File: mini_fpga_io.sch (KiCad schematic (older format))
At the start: 1 part

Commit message: First checkover of schematic complete, should be working.
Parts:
- added D? (x3): LED, ~, symbol LED
- added J? (x2): 1X6_HEADER, symbol 1X6_HEADER
- added R? (x3): 330, ~, symbol R
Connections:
- net at U?.F11 (IO_L31P_A19_M1CKE_1): now also D?.1 (A)
- net at U?.F12 (IO_L31N_A18_M1A12_1): now also D?.1 (A)
- net at U?.F13 (IO_L39P_M1A3_1): now also J?.1 (D1)
- net at U?.F15 (IO_L39N_M1ODT_1): now also J?.2 (D2)
- net at U?.H10 (IO_L32P_A17_M1A8_1): now also D?.1 (A)
- net at U?.K12 (IO_L40P_GCLK11_M1A5_1): now also J?.3 (D3)
- net at U?.L12 (IO_L40N_GCLK10_M1A6_1): now also J?.4 (D4)
- net at U?.L14 (IO_L45P_A1_M1LDQS_1): now also J?.1 (D1)
- net at U?.L15 (IO_L45N_A0_M1LDQSN_1): now also J?.2 (D2)
- net at U?.M13 (IO_L46P_FCS_B_M1DQ2_1): now also J?.3 (D3)
- net at U?.M15 (IO_L46N_FOE_B_M1DQ3_1): now also J?.4 (D4)
- new net: D?.2 (K), R?.2 (x3)
- new net +3.3V: J?.6 (VCC), J?.6 (VCC)
- new net GND: J?.5 (GND), J?.5 (GND), R?.1, R?.1, R?.1
- no-connect marks 1 -> 29
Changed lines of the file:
@@
 Sheet 4 6
 Title ""
-Date "26 jul 2014"
+Date "28 jul 2014"
 Rev ""
 Comp ""
@@
 $EndComp
 NoConn ~ 8700 4800
+$Comp
+L 1X6_HEADER J?
+U 1 1 53D596A7
+P 10200 2250
+F 0 "J?" H 10250 2650 60  0000 C CNN
+F 1 "1X6_HEADER" H 10350 1850 60  0000 C CNN
+F 2 "" H 10300 2000 60  0000 C CNN
+F 3 "" H 10300 2000 60  0000 C CNN
+	1    10200 2250
+	1    0    0    -1
+$EndComp
+$Comp
+L 1X6_HEADER J?
+U 1 1 53D596B4
+P 10200 4050
+F 0 "J?" H 10250 4450 60  0000 C CNN
+F 1 "1X6_HEADER" H 10350 3650 60  0000 C CNN
+F 2 "" H 10300 3800 60  0000 C CNN
+F 3 "" H 10300 3800 60  0000 C CNN
+	1    10200 4050
+	1    0    0    -1
+$EndComp
+Wire Wire Line
+	9900 3800 8700 3800
+Wire Wire Line
+	9900 3900 8700 3900
+Wire Wire Line
+	9900 4000 8850 4000
+Wire Wire Line
+	8850 4000 8850 4100
+Wire Wire Line
+	8850 4100 8700 4100
+Wire Wire Line
+	9900 4100 8950 4100
+Wire Wire Line
+	8950 4100 8950 4200
+Wire Wire Line
+	8950 4200 8700 4200
+Wire Wire Line
+	9900 4200 9050 4200
+Wire Wire Line
+	9050 2400 9050 4350
+Wire Wire Line
+	9800 4300 9900 4300
+Wire Wire Line
+	9800 2500 9800 4300
+Wire Wire Line
+	9900 2000 8700 2000
+Wire Wire Line
+	9900 2100 8700 2100
+Wire Wire Line
+	9900 2200 8850 2200
+Wire Wire Line
+	8850 2200 8850 2300
+Wire Wire Line
+	8850 2300 8700 2300
+Wire Wire Line
+	9900 2300 8950 2300
+Wire Wire Line
+	8950 2300 8950 2400
+Wire Wire Line
+	8950 2400 8700 2400
+Wire Wire Line
+	9900 2500 9800 2500
+$Comp
+L +3.3V #PWR?
+U 1 1 53D59B4F
+P 10250 3100
+F 0 "#PWR?" H 10250 3060 30  0001 C CNN
+F 1 "+3.3V" H 10250 3210 30  0000 C CNN
+F 2 "" H 10250 3100 60  0000 C CNN
+F 3 "" H 10250 3100 60  0000 C CNN
+	1    10250 3100
+	1    0    0    -1
+$EndComp
+Wire Wire Line
+	10250 3100 10250 3200
+Wire Wire Line
+	10250 3200 9800 3200
+Connection ~ 9800 3200
+Wire Wire Line
+	9900 2400 9050 2400
+Connection ~ 9050 4200
+$Comp
+L GND #PWR?
+U 1 1 53D59B8D
+P 9050 4350
+F 0 "#PWR?" H 9050 4350 30  0001 C CNN
+F 1 "GND" H 9050 4280 30  0001 C CNN
+F 2 "" H 9050 4350 60  0000 C CNN
+F 3 "" H 9050 4350 60  0000 C CNN
+	1    9050 4350
+	1    0    0    -1
+$EndComp
+NoConn ~ 8700 2600
+NoConn ~ 8700 2700
+NoConn ~ 8700 2900
+NoConn ~ 8700 3000
+NoConn ~ 8700 3200
+NoConn ~ 8700 3300
+NoConn ~ 8700 3500
+NoConn ~ 8700 3600
+NoConn ~ 8700 4400
+NoConn ~ 8700 4500
+NoConn ~ 8700 4700
+NoConn ~ 5700 4800
+NoConn ~ 5700 4700
+NoConn ~ 5700 4500
+NoConn ~ 5700 4400
+NoConn ~ 5700 4200
+NoConn ~ 5700 4100
+NoConn ~ 5700 3900
+NoConn ~ 5700 3800
+NoConn ~ 5700 3600
+NoConn ~ 5700 3500
+NoConn ~ 5700 3300
+NoConn ~ 5700 3200
+NoConn ~ 5700 3000
+NoConn ~ 5700 2400
+NoConn ~ 5700 2300
+NoConn ~ 5700 2100
+NoConn ~ 5700 2000
+$Comp
+L LED D?
+U 1 1 53D5A712
+P 4900 2600
+F 0 "D?" H 4900 2700 50  0000 C CNN
+F 1 "LED" H 4900 2500 50  0000 C CNN
+F 2 "~" H 4900 2600 60  0000 C CNN
+F 3 "~" H 4900 2600 60  0000 C CNN
+	1    4900 2600
+	-1   0    0    1
+$EndComp
+$Comp
+L LED D?
+U 1 1 53D5A71F
+P 4900 2900
+F 0 "D?" H 4900 3000 50  0000 C CNN
+F 1 "LED" H 4900 2800 50  0000 C CNN
+F 2 "~" H 4900 2900 60  0000 C CNN
+F 3 "~" H 4900 2900 60  0000 C CNN
+	1    4900 2900
+	-1   0    0    1
+$EndComp
+$Comp
+L LED D?
+U 1 1 53D5A725
+P 4900 3200
+F 0 "D?" H 4900 3300 50  0000 C CNN
+F 1 "LED" H 4900 3100 50  0000 C CNN
+F 2 "~" H 4900 3200 60  0000 C CNN
+F 3 "~" H 4900 3200 60  0000 C CNN
+	1    4900 3200
+	-1   0    0    1
+$EndComp
+$Comp
+L GND #PWR?
+U 1 1 53D5A72D
+P 3650 3500
+F 0 "#PWR?" H 3650 3500 30  0001 C CNN
+F 1 "GND" H 3650 3430 30  0001 C CNN
+F 2 "" H 3650 3500 60  0000 C CNN
+F 3 "" H 3650 3500 60  0000 C CNN
+	1    3650 3500
+	1    0    0    -1
+$EndComp
+$Comp
+L R R?
+U 1 1 53D5A73C
+P 4100 2600
+F 0 "R?" V 4180 2600 40  0000 C CNN
+F 1 "330" V 4107 2601 40  0000 C CNN
+F 2 "~" V 4030 2600 30  0000 C CNN
+F 3 "~" H 4100 2600 30  0000 C CNN
+	1    4100 2600
+	0    -1   -1   0
+$EndComp
+Wire Wire Line
+	3850 2600 3650 2600
+Wire Wire Line
+	3650 2600 3650 3500
+Wire Wire Line
+	3850 2900 3650 2900
+Connection ~ 3650 2900
+Wire Wire Line
+	3850 3200 3650 3200
+Connection ~ 3650 3200
+Wire Wire Line
+	4700 2600 4350 2600
+$Comp
+L R R?
+U 1 1 53D5A7E5
+P 4100 2900
+F 0 "R?" V 4180 2900 40  0000 C CNN
+F 1 "330" V 4107 2901 40  0000 C CNN
+F 2 "~" V 4030 2900 30  0000 C CNN
+F 3 "~" H 4100 2900 30  0000 C CNN
+	1    4100 2900
+	0    -1   -1   0
+$EndComp
+$Comp
+L R R?
+U 1 1 53D5A7EB
+P 4100 3200
+F 0 "R?" V 4180 3200 40  0000 C CNN
+F 1 "330" V 4107 3201 40  0000 C CNN
+F 2 "~" V 4030 3200 30  0000 C CNN
+F 3 "~" H 4100 3200 30  0000 C CNN
+	1    4100 3200
+	0    -1   -1   0
+$EndComp
+Wire Wire Line
+	4350 2900 4700 2900
+Wire Wire Line
+	4350 3200 4700 3200
+Wire Wire Line
+	5100 2600 5700 2600
+Wire Wire Line
+	5100 2900 5100 2700
+Wire Wire Line
+	5100 2700 5700 2700
+Wire Wire Line
+	5100 3200 5200 3200
+Wire Wire Line
+	5200 3200 5200 2900
+Wire Wire Line
+	5200 2900 5700 2900
 $EndSCHEMATC

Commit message: Annotated!
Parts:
- gave numbers to parts that had none: 9
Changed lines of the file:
@@
 $EndDescr
 $Comp
-L XC6SLX9 U?
+L XC6SLX9 U3
 U 4 1 53CA82DC
 P 7200 3250
-F 0 "U?" H 7200 3150 60  0000 C CNN
+F 0 "U3" H 7200 3150 60  0000 C CNN
 F 1 "XC6SLX9" H 7200 3350 60  0000 C CNN
 F 2 "~" H 7350 5250 60  0000 C CNN
@@
 NoConn ~ 8700 4800
 $Comp
-L 1X6_HEADER J?
+L 1X6_HEADER J2
 U 1 1 53D596A7
 P 10200 2250
-F 0 "J?" H 10250 2650 60  0000 C CNN
+F 0 "J2" H 10250 2650 60  0000 C CNN
 F 1 "1X6_HEADER" H 10350 1850 60  0000 C CNN
 F 2 "" H 10300 2000 60  0000 C CNN
@@
 $EndComp
 $Comp
-L 1X6_HEADER J?
+L 1X6_HEADER J3
 U 1 1 53D596B4
 P 10200 4050
-F 0 "J?" H 10250 4450 60  0000 C CNN
+F 0 "J3" H 10250 4450 60  0000 C CNN
 F 1 "1X6_HEADER" H 10350 3650 60  0000 C CNN
 F 2 "" H 10300 3800 60  0000 C CNN
@@
 	9900 2500 9800 2500
 $Comp
-L +3.3V #PWR?
+L +3.3V #PWR39
 U 1 1 53D59B4F
 P 10250 3100
-F 0 "#PWR?" H 10250 3060 30  0001 C CNN
+F 0 "#PWR39" H 10250 3060 30  0001 C CNN
 F 1 "+3.3V" H 10250 3210 30  0000 C CNN
 F 2 "" H 10250 3100 60  0000 C CNN
@@
 Connection ~ 9050 4200
 $Comp
-L GND #PWR?
+L GND #PWR38
 U 1 1 53D59B8D
 P 9050 4350
-F 0 "#PWR?" H 9050 4350 30  0001 C CNN
+F 0 "#PWR38" H 9050 4350 30  0001 C CNN
 F 1 "GND" H 9050 4280 30  0001 C CNN
 F 2 "" H 9050 4350 60  0000 C CNN
@@
 NoConn ~ 5700 2000
 $Comp
-L LED D?
+L LED D2
 U 1 1 53D5A712
 P 4900 2600
-F 0 "D?" H 4900 2700 50  0000 C CNN
+F 0 "D2" H 4900 2700 50  0000 C CNN
 F 1 "LED" H 4900 2500 50  0000 C CNN
 F 2 "~" H 4900 2600 60  0000 C CNN
@@
 $EndComp
 $Comp
-L LED D?
+L LED D3
 U 1 1 53D5A71F
 P 4900 2900
-F 0 "D?" H 4900 3000 50  0000 C CNN
+F 0 "D3" H 4900 3000 50  0000 C CNN
 F 1 "LED" H 4900 2800 50  0000 C CNN
 F 2 "~" H 4900 2900 60  0000 C CNN
@@
 $EndComp
 $Comp
-L LED D?
+L LED D4
 U 1 1 53D5A725
 P 4900 3200
-F 0 "D?" H 4900 3300 50  0000 C CNN
+F 0 "D4" H 4900 3300 50  0000 C CNN
 F 1 "LED" H 4900 3100 50  0000 C CNN
 F 2 "~" H 4900 3200 60  0000 C CNN
@@
 $EndComp
 $Comp
-L GND #PWR?
+L GND #PWR37
 U 1 1 53D5A72D
 P 3650 3500
-F 0 "#PWR?" H 3650 3500 30  0001 C CNN
+F 0 "#PWR37" H 3650 3500 30  0001 C CNN
 F 1 "GND" H 3650 3430 30  0001 C CNN
 F 2 "" H 3650 3500 60  0000 C CNN
@@
 $EndComp
 $Comp
-L R R?
+L R R40
 U 1 1 53D5A73C
 P 4100 2600
-F 0 "R?" V 4180 2600 40  0000 C CNN
+F 0 "R40" V 4180 2600 40  0000 C CNN
 F 1 "330" V 4107 2601 40  0000 C CNN
 F 2 "~" V 4030 2600 30  0000 C CNN
@@
 	4700 2600 4350 2600
 $Comp
-L R R?
+L R R41
 U 1 1 53D5A7E5
 P 4100 2900
-F 0 "R?" V 4180 2900 40  0000 C CNN
+F 0 "R41" V 4180 2900 40  0000 C CNN
 F 1 "330" V 4107 2901 40  0000 C CNN
 F 2 "~" V 4030 2900 30  0000 C CNN
@@
 $EndComp
 $Comp
-L R R?
+L R R42
 U 1 1 53D5A7EB
 P 4100 3200
-F 0 "R?" V 4180 3200 40  0000 C CNN
+F 0 "R42" V 4180 3200 40  0000 C CNN
 F 1 "330" V 4107 3201 40  0000 C CNN
 F 2 "~" V 4030 3200 30  0000 C CNN

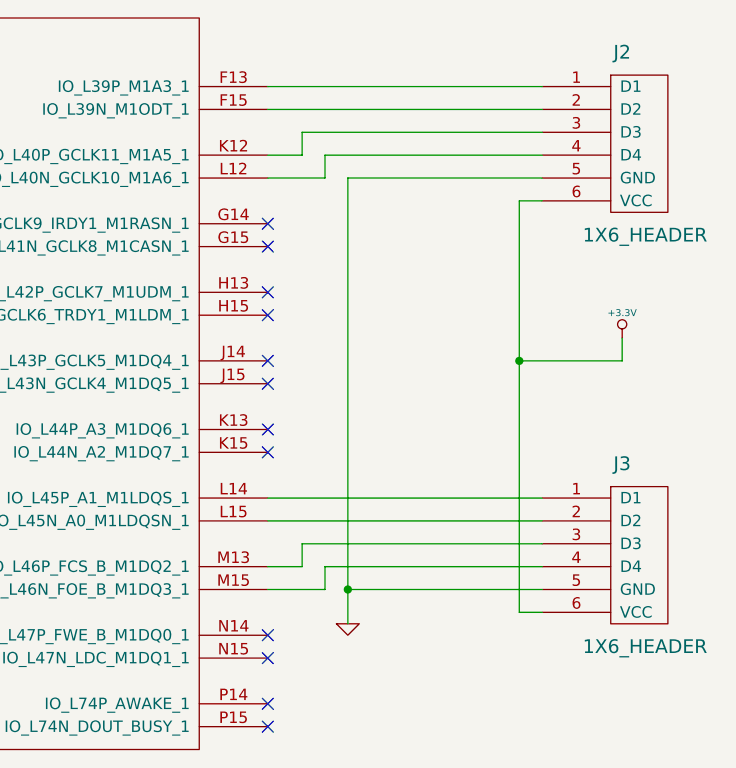
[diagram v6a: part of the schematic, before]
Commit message: minor edits to components to fix some pin assignment issues.
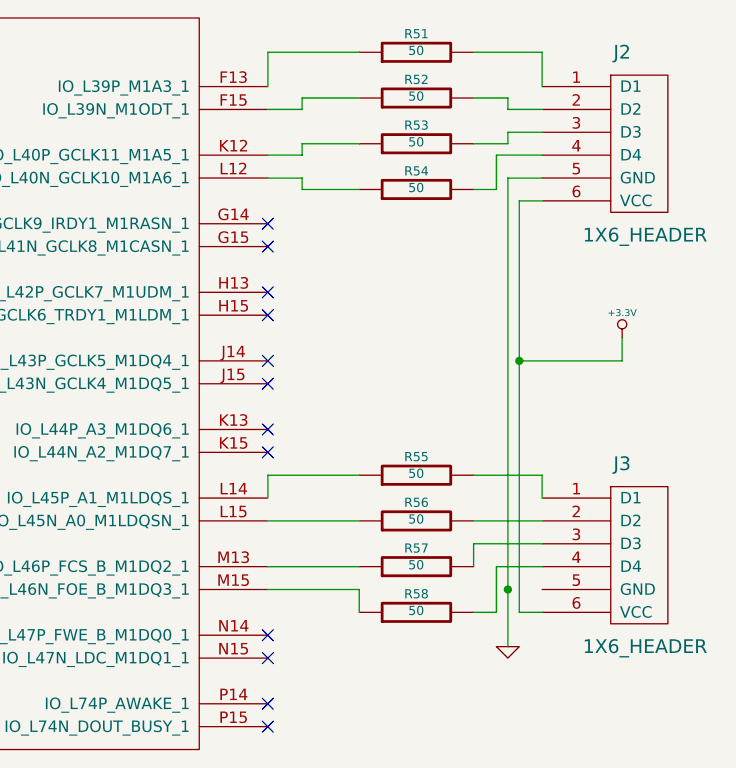
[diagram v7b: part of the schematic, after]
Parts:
- added R51, R52, R53, R54, R55, R56, R57, R58: 50, ~, symbol R
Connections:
- net GND: no longer J3.5 (GND)
- net at U3.F13 (IO_L39P_M1A3_1): now also R51.1; no longer J2.1 (D1)
- net at U3.F15 (IO_L39N_M1ODT_1): now also R52.1; no longer J2.2 (D2)
- net at U3.K12 (IO_L40P_GCLK11_M1A5_1): now also R53.1; no longer J2.3 (D3)
- net at U3.L12 (IO_L40N_GCLK10_M1A6_1): now also R54.1; no longer J2.4 (D4)
- net at U3.L14 (IO_L45P_A1_M1LDQS_1): now also R55.1; no longer J3.1 (D1)
- net at U3.L15 (IO_L45N_A0_M1LDQSN_1): now also R56.1; no longer J3.2 (D2)
- net at U3.M13 (IO_L46P_FCS_B_M1DQ2_1): now also R57.1; no longer J3.3 (D3)
- net at U3.M15 (IO_L46N_FOE_B_M1DQ3_1): now also R58.1; no longer J3.4 (D4)
- new net: J2.1 (D1), R51.2
- new net: J2.2 (D2), R52.2
- new net: J2.3 (D3), R53.2
- new net: J2.4 (D4), R54.2
- new net: J3.1 (D1), R55.2
- new net: J3.2 (D2), R56.2
- new net: J3.3 (D3), R57.2
- new net: J3.4 (D4), R58.2
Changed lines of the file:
@@
 $EndComp
 Wire Wire Line
-	9900 3800 8700 3800
-Wire Wire Line
-	9900 3900 8700 3900
-Wire Wire Line
-	9900 4000 8850 4000
-Wire Wire Line
-	8850 4000 8850 4100
-Wire Wire Line
-	8850 4100 8700 4100
-Wire Wire Line
-	9900 4100 8950 4100
-Wire Wire Line
-	8950 4100 8950 4200
-Wire Wire Line
-	8950 4200 8700 4200
-Wire Wire Line
-	9900 4200 9050 4200
-Wire Wire Line
-	9050 2400 9050 4350
+	8700 4100 9100 4100
 Wire Wire Line
 	9800 4300 9900 4300
 Wire Wire Line
 	9800 2500 9800 4300
-Wire Wire Line
-	9900 2000 8700 2000
-Wire Wire Line
-	9900 2100 8700 2100
-Wire Wire Line
-	9900 2200 8850 2200
-Wire Wire Line
-	8850 2200 8850 2300
-Wire Wire Line
-	8850 2300 8700 2300
-Wire Wire Line
-	9900 2300 8950 2300
-Wire Wire Line
-	8950 2300 8950 2400
-Wire Wire Line
-	8950 2400 8700 2400
 Wire Wire Line
 	9900 2500 9800 2500
@@
 	10250 3200 9800 3200
 Connection ~ 9800 3200
-Wire Wire Line
-	9900 2400 9050 2400
-Connection ~ 9050 4200
 $Comp
 L GND #PWR038
 U 1 1 53D59B8D
-P 9050 4350
-F 0 "#PWR038" H 9050 4350 30  0001 C CNN
-F 1 "GND" H 9050 4280 30  0001 C CNN
-F 2 "" H 9050 4350 60  0000 C CNN
-F 3 "" H 9050 4350 60  0000 C CNN
-	1    9050 4350
+P 9750 4450
+F 0 "#PWR038" H 9750 4450 30  0001 C CNN
+F 1 "GND" H 9750 4380 30  0001 C CNN
+F 2 "" H 9750 4450 60  0000 C CNN
+F 3 "" H 9750 4450 60  0000 C CNN
+	1    9750 4450
 	1    0    0    -1
 $EndComp
@@
 Wire Wire Line
 	5200 2900 5700 2900
+$Comp
+L R R51
+U 1 1 53D6CE69
+P 9350 1850
+F 0 "R51" V 9430 1850 40  0000 C CNN
+F 1 "50" V 9357 1851 40  0000 C CNN
+F 2 "~" V 9280 1850 30  0000 C CNN
+F 3 "~" H 9350 1850 30  0000 C CNN
+	1    9350 1850
+	0    -1   -1   0
+$EndComp
+$Comp
+L R R52
+U 1 1 53D6CE89
+P 9350 2050
+F 0 "R52" V 9430 2050 40  0000 C CNN
+F 1 "50" V 9357 2051 40  0000 C CNN
+F 2 "~" V 9280 2050 30  0000 C CNN
+F 3 "~" H 9350 2050 30  0000 C CNN
+	1    9350 2050
+	0    -1   -1   0
+$EndComp
+$Comp
+L R R53
+U 1 1 53D6CE8F
+P 9350 2250
+F 0 "R53" V 9430 2250 40  0000 C CNN
+F 1 "50" V 9357 2251 40  0000 C CNN
+F 2 "~" V 9280 2250 30  0000 C CNN
+F 3 "~" H 9350 2250 30  0000 C CNN
+	1    9350 2250
+	0    -1   -1   0
+$EndComp
+$Comp
+L R R54
+U 1 1 53D6CE95
+P 9350 2450
+F 0 "R54" V 9430 2450 40  0000 C CNN
+F 1 "50" V 9357 2451 40  0000 C CNN
+F 2 "~" V 9280 2450 30  0000 C CNN
+F 3 "~" H 9350 2450 30  0000 C CNN
+	1    9350 2450
+	0    -1   -1   0
+$EndComp
+Wire Wire Line
+	9900 2100 9750 2100
+Wire Wire Line
+	9750 2100 9750 2050
+Wire Wire Line
+	9750 2050 9600 2050
+Wire Wire Line
+	9100 2050 8850 2050
+Wire Wire Line
+	8850 2050 8850 2100
+Wire Wire Line
+	8850 2100 8700 2100
+Wire Wire Line
+	9900 2200 9750 2200
+Wire Wire Line
+	9750 2200 9750 2250
+Wire Wire Line
+	9750 2250 9600 2250
+Wire Wire Line
+	9100 2250 8850 2250
+Wire Wire Line
+	8850 2250 8850 2300
+Wire Wire Line
+	8850 2300 8700 2300
+Wire Wire Line
+	9900 2000 9900 1850
+Wire Wire Line
+	9900 1850 9600 1850
+Wire Wire Line
+	9100 1850 8700 1850
+Wire Wire Line
+	8700 1850 8700 2000
+Wire Wire Line
+	9900 2300 9700 2300
+Wire Wire Line
+	9700 2300 9700 2450
+Wire Wire Line
+	9700 2450 9600 2450
+Wire Wire Line
+	9100 2450 8850 2450
+Wire Wire Line
+	8850 2450 8850 2400
+Wire Wire Line
+	8850 2400 8700 2400
+Wire Wire Line
+	9900 2400 9750 2400
+Wire Wire Line
+	9750 2400 9750 4450
+Connection ~ 9750 4200
+$Comp
+L R R55
+U 1 1 53D6D12C
+P 9350 3700
+F 0 "R55" V 9430 3700 40  0000 C CNN
+F 1 "50" V 9357 3701 40  0000 C CNN
+F 2 "~" V 9280 3700 30  0000 C CNN
+F 3 "~" H 9350 3700 30  0000 C CNN
+	1    9350 3700
+	0    -1   -1   0
+$EndComp
+$Comp
+L R R56
+U 1 1 53D6D132
+P 9350 3900
+F 0 "R56" V 9430 3900 40  0000 C CNN
+F 1 "50" V 9357 3901 40  0000 C CNN
+F 2 "~" V 9280 3900 30  0000 C CNN
+F 3 "~" H 9350 3900 30  0000 C CNN
+	1    9350 3900
+	0    -1   -1   0
+$EndComp
+$Comp
+L R R57
+U 1 1 53D6D138
+P 9350 4100
+F 0 "R57" V 9430 4100 40  0000 C CNN
+F 1 "50" V 9357 4101 40  0000 C CNN
+F 2 "~" V 9280 4100 30  0000 C CNN
+F 3 "~" H 9350 4100 30  0000 C CNN
+	1    9350 4100
+	0    -1   -1   0
+$EndComp
+$Comp
+L R R58
+U 1 1 53D6D13E
+P 9350 4300
+F 0 "R58" V 9430 4300 40  0000 C CNN
+F 1 "50" V 9357 4301 40  0000 C CNN
+F 2 "~" V 9280 4300 30  0000 C CNN
+F 3 "~" H 9350 4300 30  0000 C CNN
+	1    9350 4300
+	0    -1   -1   0
+$EndComp
+Wire Wire Line
+	9900 3800 9900 3700
+Wire Wire Line
+	9900 3700 9600 3700
+Wire Wire Line
+	9100 3700 8700 3700
+Wire Wire Line
+	8700 3700 8700 3800
+Wire Wire Line
+	9900 3900 9600 3900
+Wire Wire Line
+	9100 3900 8700 3900
+Wire Wire Line
+	9900 4000 9600 4000
+Wire Wire Line
+	9600 4000 9600 4100
+Wire Wire Line
+	9900 4100 9700 4100
+Wire Wire Line
+	9700 4100 9700 4300
+Wire Wire Line
+	9700 4300 9600 4300
+Wire Wire Line
+	9100 4300 9100 4200
+Wire Wire Line
+	9100 4200 8700 4200
 $EndSCHEMATC
